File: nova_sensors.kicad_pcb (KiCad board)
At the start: 2 copper layers, 100 x 82.5 mm, 93 parts, among them J1 Conn_01x03_Socket, J10 Conn_01x04_Socket, J11 Conn_01x04_Socket, J2 Conn_01x03_Socket, J3 Conn_01x04_Socket, J4 Conn_01x02_Socket, J5 Conn_01x02_Socket, J6 Conn_01x03_Socket, J7 Conn_01x02_Socket, J8 Conn_01x02_Socket, J9 Conn_01x02_Socket, SW1 SW_Push, SW2 SW_DIP_x02, SW3 SW_DIP_x02, U1 AT32F455CET7, U2 MAX3232, U3 MAX13488, U4 MAX13488, U5 LD1117S33TR, U6 XL1509-ADJ, Y1 8Mhz, Y2 32768hz

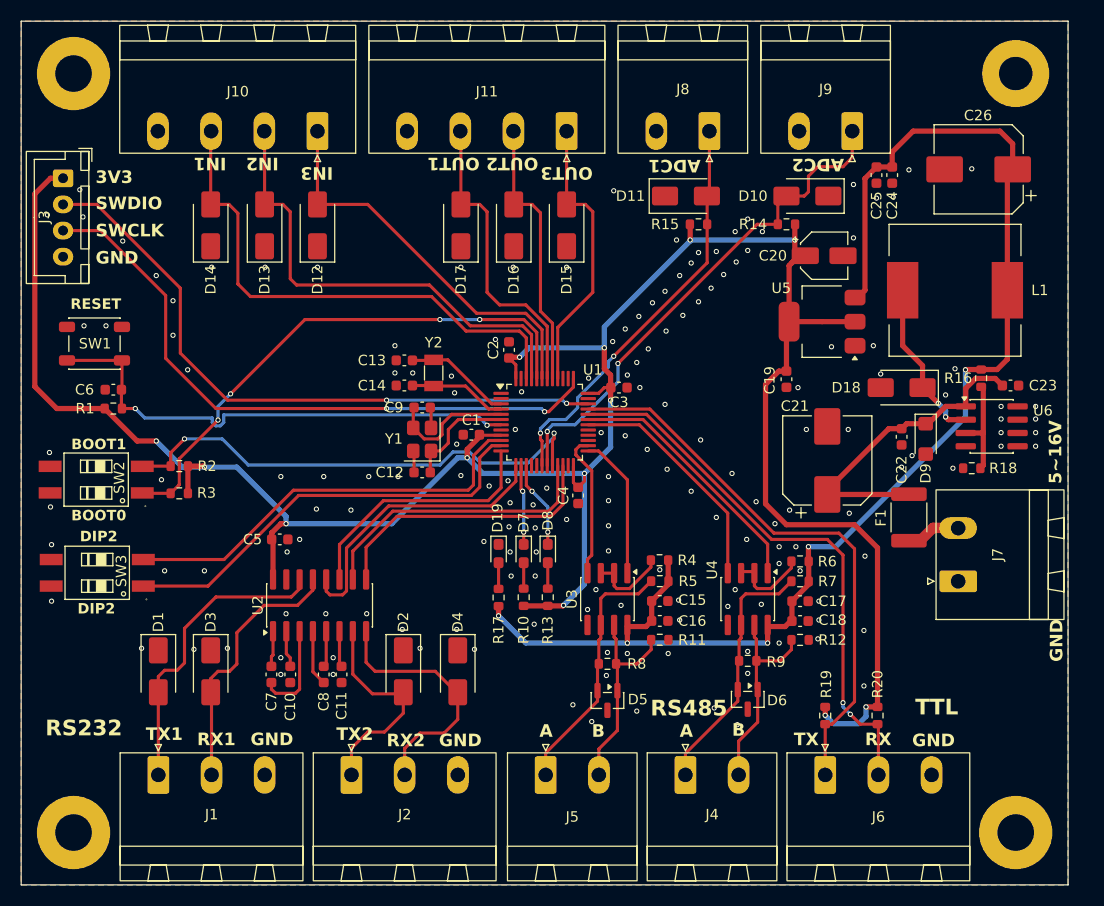
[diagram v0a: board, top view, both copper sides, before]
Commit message: fix: 修改ADC电路，将RL分压方向改为接地端；mcu侧增加限流电阻和滤波电容；Rx侧增加滤波电容
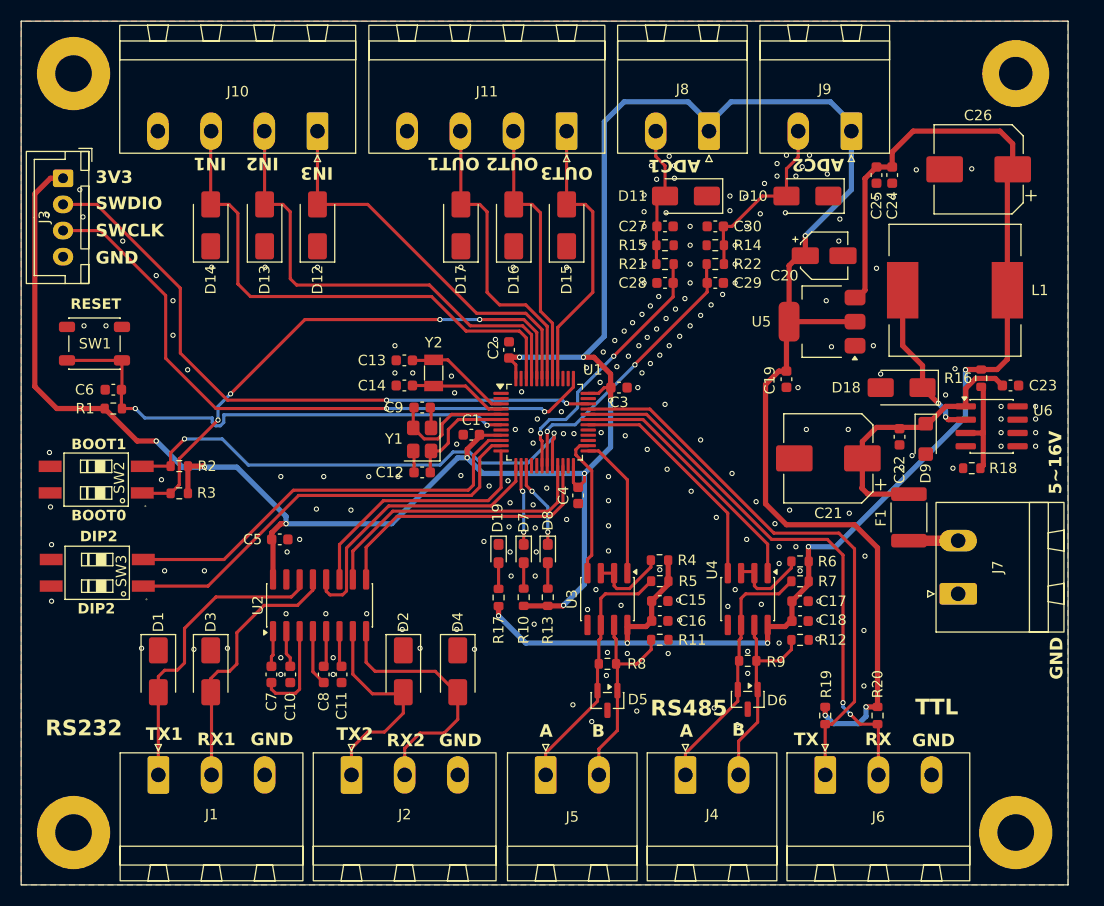
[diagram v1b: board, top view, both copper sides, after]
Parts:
- added C27: 1uF, Capacitor_SMD:C_0603_1608Metric, F.Cu at (61.5, 147.1)
- added C28: 100nF, Capacitor_SMD:C_0603_1608Metric, F.Cu at (61.5, 152.5)
- added C29: 100nF, Capacitor_SMD:C_0603_1608Metric, F.Cu at (66.3, 152.5)
- added C30: 1uF, Capacitor_SMD:C_0603_1608Metric, F.Cu at (66.3, 147.1)
- added R21: 1K, Resistor_SMD:R_0603_1608Metric, F.Cu at (61.5, 150.7)
- added R22: 1K, Resistor_SMD:R_0603_1608Metric, F.Cu at (66.3, 150.7)
- J8, J9: value Conn_01x02_Socket -> 01x02_Socket
- R14, R15: value 10K -> 1K5/1%
- moved R14 7.09 mm to (66.3, 148.9)
- moved R15 3.77 mm to (61.5, 148.9)
- moved J7 1.20 mm to (89.5, 182.2)
- moved C21 0.22 mm to (77.1, 169.3), turned to 180 degrees
- moved C22 0.20 mm to (83.9, 167.2)
- moved J9 0.08 mm to (79.3, 138.0)
- turned D11 to 180 degrees
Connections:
- D10 pad 2: /ADC2 -> Net-(D10-A2)
- D11 pad 2: /ADC1 -> Net-(D11-A2)
- J8 pad 1: /ADC1 -> +3V3
- J8 pad 2: GND -> Net-(D11-A2)
- J9 pad 1: /ADC2 -> +3V3
- J9 pad 2: GND -> Net-(D10-A2)
- R14 pad 1: +3V3 -> Net-(D10-A2)
- R14 pad 2: /ADC2 -> GND
- R15 pad 1: +3V3 -> Net-(D11-A2)
- R15 pad 2: /ADC1 -> GND
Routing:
- net +3V3: track 244.1 -> 279.4 mm, vias 13 -> 12
- net /ADC2: track 48.7 -> 26.7 mm
- net Net-(D10-A2): track 0.00 -> 17.5 mm
- net /ADC1: track 39.6 -> 25.5 mm
- net Net-(D11-A2): track 0.00 -> 13.4 mm
- net 4V5~16V: track 30.7 -> 26.5 mm
- net Net-(J7-Pin_2): track 5.22 -> 4.70 mm
- net GND: vias 169 -> 211

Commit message: fix: 调整丝印位置
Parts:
- J7: value Conn_01x02_Socket -> 01x02_Socket
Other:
- board text added: "A1"
- board text added: "A2"
- board text added: "B1"
- board text added: "B2"
- board text added: "USART(+3V3)"
- board text removed: "A"
- board text removed: "B"
- board text removed: "TTL"

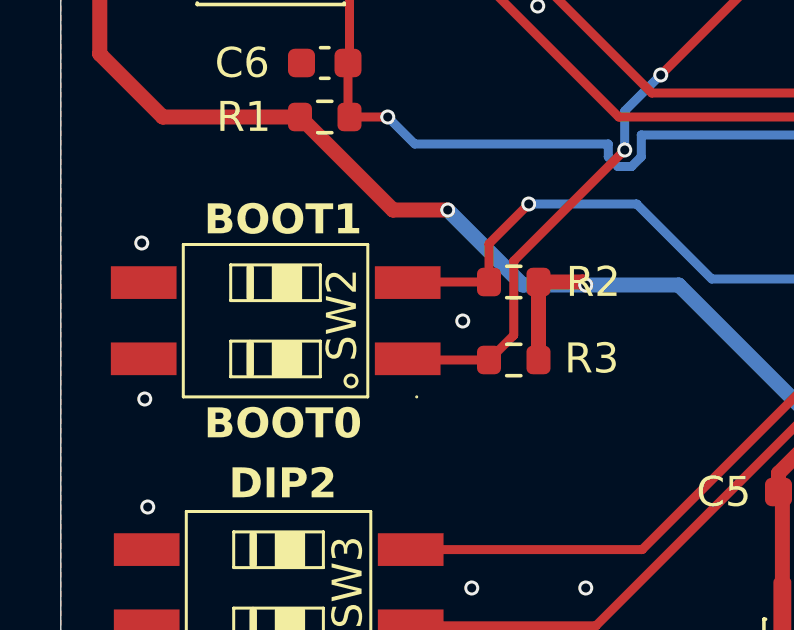
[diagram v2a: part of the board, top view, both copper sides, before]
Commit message: doc: 修改原理图版本，生成各种生产资料
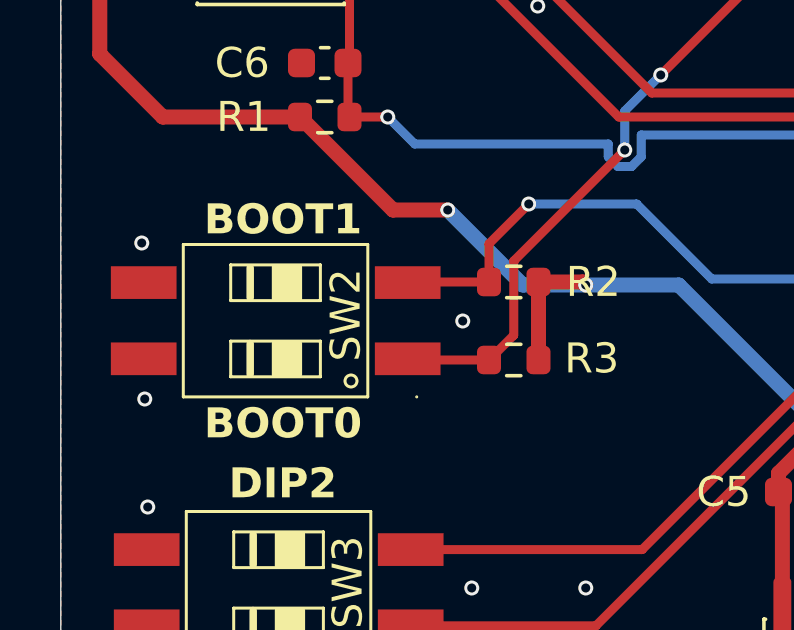
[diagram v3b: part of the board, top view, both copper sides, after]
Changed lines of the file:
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@@
 		(descr "2.54-2P TPGT")
 		(property "Reference" "SW2"
-			(at 0.2 2.2 90)
+			(at 0.2 2.325 90)
 			(layer "F.SilkS")
 			(effects

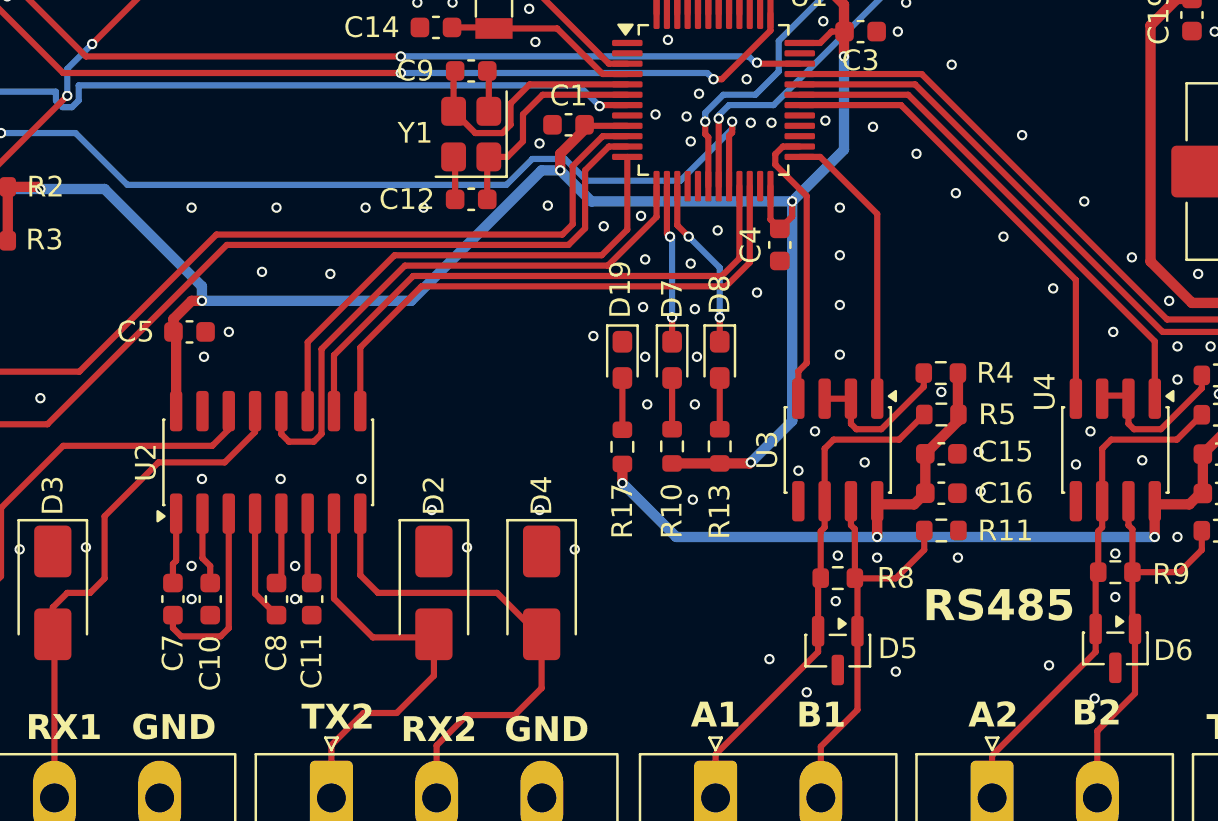
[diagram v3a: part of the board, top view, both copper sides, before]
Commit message: fix: 调整一处3.3V走线和过孔
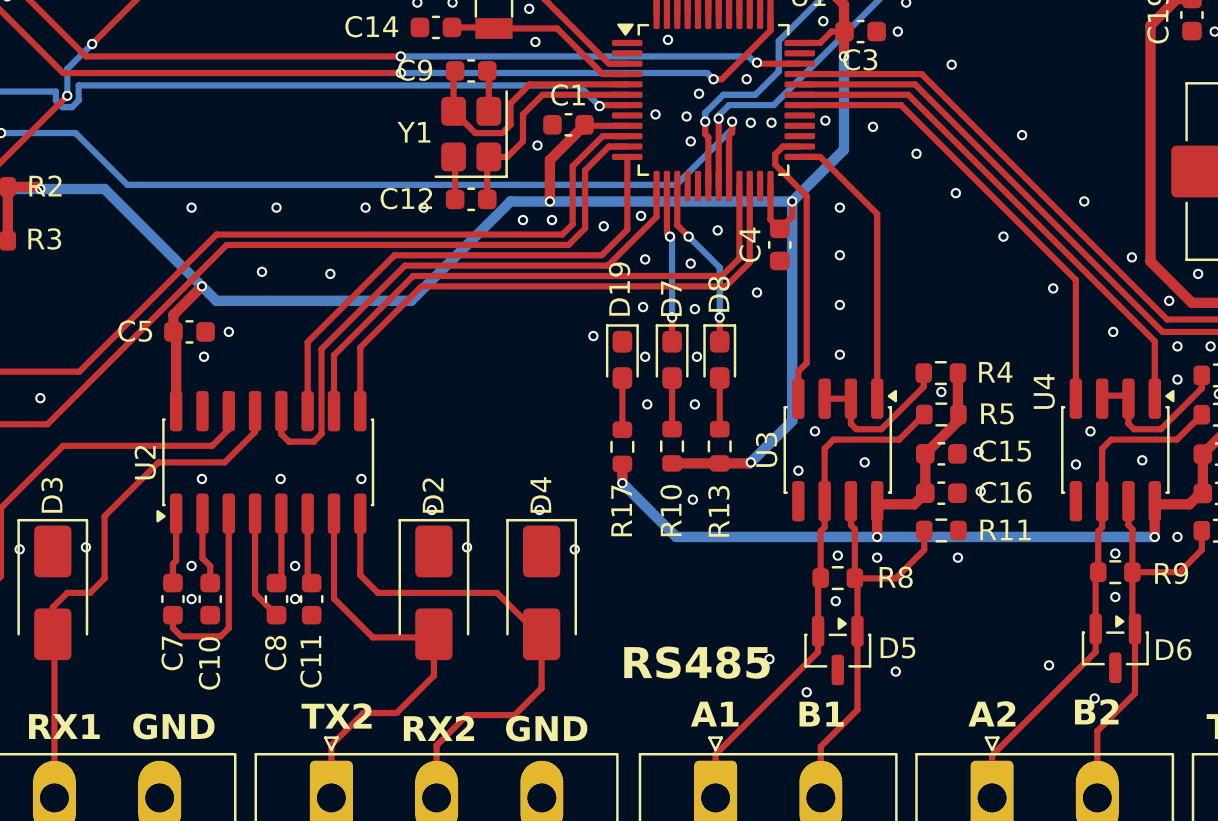
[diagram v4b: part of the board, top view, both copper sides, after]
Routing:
- net /BOOT1: track 47.7 -> 46.8 mm
- net +3V3: track 279.4 -> 280.0 mm
- net GND: vias 211 -> 212
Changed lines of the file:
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@@
 	)
 	(gr_text "RS485"
-		(at 60.1 191.1 0)
+		(at 45.5 193.9 0)
 		(layer "F.SilkS")
 		(effects
@@
 	)
 	(via
+		(at 40.8 171.6)
+		(size 0.5)
+		(drill 0.3)
+		(layers "F.Cu" "B.Cu")
+		(free yes)
+		(net "GND")
+	)
+	(via
 		(at 73.4 174.2)
 		(size 0.5)
@@
 	)
 	(via
-		(at 42 170.9)
-		(size 0.5)
-		(drill 0.3)
-		(layers "F.Cu" "B.Cu")
-		(free yes)
-		(net "GND")
-	)
-	(via
 		(at 2.7 168.7)
 		(size 0.5)
@@
 	)
 	(via
-		(at 41.6 167.9)
+		(at 41.5 168)
 		(size 0.5)
 		(drill 0.3)
@@
 	)
 	(via
+		(at 42.2 171.6)
+		(size 0.5)
+		(drill 0.3)
+		(layers "F.Cu" "B.Cu")
+		(free yes)
+		(net "GND")
+	)
+	(via
 		(at 66.2 193.1)
 		(size 0.5)
@@
 	)
 	(segment
-		(start 25.3 175.5)
-		(end 24.8 175.5)
+		(start 11.075 167.6)
+		(end 12.9 167.6)
 		(width 0.5)
 		(layer "F.Cu")
@@
 	)
 	(segment
-		(start 11.075 167.6)
-		(end 12.9 167.6)
+		(start 73.1 175.6)
+		(end 71.1 173.6)
 		(width 0.5)
 		(layer "F.Cu")
@@
 	)
 	(segment
-		(start 73.1 175.6)
-		(end 71.1 173.6)
+		(start 42.1 170.7)
+		(end 42.1 168.7)
 		(width 0.5)
 		(layer "F.Cu")
@@
 	)
 	(segment
-		(start 24.8 175.5)
-		(end 23.925 176.375)
+		(start 42.1 168.7)
+		(end 43.575 167.225)
 		(width 0.5)
 		(layer "F.Cu")
@@
 	)
 	(segment
-		(start 23.925 176.375)
-		(end 23.925 177)
-		(width 0.5)
-		(layer "F.Cu")
-		(net "+3V3")
-	)
-	(segment
 		(start 17.4 170)
 		(end 17.5 170.1)
@@
 	)
 	(segment
-		(start 42.6 168.4)
-		(end 42.6 169.2)
-		(width 0.5)
-		(layer "F.Cu")
-		(net "+3V3")
-	)
-	(segment
 		(start 76.8 193.8)
 		(end 76.8 193)
@@
 	)
 	(segment
-		(start 43.775 167.225)
-		(end 42.6 168.4)
-		(width 0.5)
-		(layer "F.Cu")
-		(net "+3V3")
-	)
-	(segment
 		(start 24.055 180.825)
 		(end 24.055 177.13)
@@
 	)
 	(segment
+		(start 25.3 174.8)
+		(end 23.925 176.175)
+		(width 0.5)
+		(layer "F.Cu")
+		(net "+3V3")
+	)
+	(segment
 		(start 75.375 149.425)
 		(end 74.9 149.9)
@@
 	)
 	(segment
+		(start 23.925 176.175)
+		(end 23.925 177)
+		(width 0.5)
+		(layer "F.Cu")
+		(net "+3V3")
+	)
+	(segment
 		(start 4 142.5)
 		(end 2.8 142.5)
@@
 		(net "+3V3")
 	)
+	(segment
+		(start 43.575 167.225)
+		(end 43.775 167.225)
+		(width 0.5)
+		(layer "F.Cu")
+		(net "+3V3")
+	)
 	(via
 		(at 53.7 159.6)
@@
 	)
 	(via
-		(at 42.6 169.2)
+		(at 42.1 170.7)
 		(size 0.5)
 		(drill 0.3)
@@
 	)
 	(via
-		(at 25.3 175.5)
+		(at 25.3 174.8)
 		(size 0.5)
 		(drill 0.3)
@@
 	)
 	(segment
-		(start 41.7 169.2)
-		(end 35.4 175.5)
+		(start 42.1 170.7)
+		(end 53.8 170.7)
 		(width 0.5)
 		(layer "B.Cu")
@@
 	)
 	(segment
-		(start 20.6 170.1)
-		(end 17.5 170.1)
+		(start 40.2 170.7)
+		(end 42.1 170.7)
+		(width 0.5)
+		(layer "B.Cu")
+		(net "+3V3")
+	)
+	(segment
+		(start 26 175.5)
+		(end 35.4 175.5)
 		(width 0.5)
 		(layer "B.Cu")
@@
 	)
 	(segment
+		(start 20.6 170.1)
+		(end 17.5 170.1)
+		(width 0.5)
+		(layer "B.Cu")
+		(net "+3V3")
+	)
+	(segment
 		(start 63.7 135.2)
 		(end 65.7 137.2)
@@
 	)
 	(segment
-		(start 42.6 169.2)
-		(end 44.1 170.7)
+		(start 15.4 170.1)
+		(end 17.5 170.1)
 		(width 0.5)
 		(layer "B.Cu")
@@
 	)
 	(segment
-		(start 15.4 170.1)
-		(end 17.5 170.1)
+		(start 80 194.6)
+		(end 80.7 193.9)
 		(width 0.5)
 		(layer "B.Cu")
@@
 	)
 	(segment
-		(start 25.3 175.5)
-		(end 25.3 174.8)
+		(start 35.4 175.5)
+		(end 40.2 170.7)
 		(width 0.5)
 		(layer "B.Cu")
@@
 	)
 	(segment
-		(start 80 194.6)
-		(end 80.7 193.9)
+		(start 25.3 174.8)
+		(end 26 175.5)
 		(width 0.5)
 		(layer "B.Cu")
@@
 	)
 	(segment
-		(start 44.1 170.7)
-		(end 53.8 170.7)
-		(width 0.5)
-		(layer "B.Cu")
-		(net "+3V3")
-	)
-	(segment
 		(start 57.6 135.2)
 		(end 63.7 135.2)
@@
 	)
 	(segment
-		(start 42.6 169.2)
-		(end 41.7 169.2)
-		(width 0.5)
-		(layer "B.Cu")
-		(net "+3V3")
-	)
-	(segment
-		(start 25.3 174.8)
-		(end 20.6 170.1)
-		(width 0.5)
-		(layer "B.Cu")
-		(net "+3V3")
-	)
-	(segment
 		(start 12.9 167.6)
 		(end 15.4 170.1)
@@
 	)
 	(segment
+		(start 25.3 174.8)
+		(end 20.6 170.1)
+		(width 0.5)
+		(layer "B.Cu")
+		(net "+3V3")
+	)
+	(segment
 		(start 77.6 194.6)
 		(end 80 194.6)
@@
 	)
 	(segment
-		(start 35.4 175.5)
-		(end 25.3 175.5)
-		(width 0.5)
-		(layer "B.Cu")
-		(net "+3V3")
-	)
-	(segment
 		(start 65.7 137.3)
 		(end 67.8 135.2)
@@
 	)
 	(segment
-		(start 50.899332 166.848611)
-		(end 50.899332 167.200668)
+		(start 19.2 167.4)
+		(end 15.6 167.4)
 		(width 0.3)
 		(layer "B.Cu")
@@
 	(segment
 		(start 50.899332 167.200668)
-		(end 48.4 169.7)
+		(end 48.2 169.9)
 		(width 0.3)
 		(layer "B.Cu")
@@
 	)
 	(segment
-		(start 19.2 167.4)
-		(end 15.6 167.4)
-		(width 0.3)
-		(layer "B.Cu")
-		(net "/BOOT1")
-	)
-	(segment
-		(start 42.827818 168.65)
-		(end 41.25 168.65)
-		(width 0.3)
-		(layer "B.Cu")
-		(net "/BOOT1")
-	)
-	(segment
-		(start 48.4 169.7)
-		(end 43.877818 169.7)
-		(width 0.3)
-		(layer "B.Cu")
-		(net "/BOOT1")
-	)
-	(segment
-		(start 40 169.9)
+		(start 48.2 169.9)
 		(end 21.7 169.9)
 		(width 0.3)
@@
 	)
 	(segment
-		(start 41.25 168.65)
-		(end 40 169.9)
+		(start 50.899332 166.848611)
+		(end 50.899332 167.200668)
 		(width 0.3)
 		(layer "B.Cu")
@@
 		(width 0.3)
 		(layer "B.Cu")
-		(net "/BOOT1")
-	)
-	(segment
-		(start 43.877818 169.7)
-		(end 42.827818 168.65)
-		(width 0.3)
-		(layer "B.Cu")

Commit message: fix: 原理图调整晶振负载电容容值和精度，PCB新增编码丝印
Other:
- board text added: "5227116 V1.0"
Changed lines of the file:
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@@
+		)
+	)
+	(gr_text "5227116 V1.0"
+		(at 12.4 157.6 0)
+		(layer "F.SilkS")
+		(effects
+			(font
+				(size 2 2)
+				(thickness 0.2)
+				(bold yes)
+			)
+			(justify left bottom)
 		)
 	)
